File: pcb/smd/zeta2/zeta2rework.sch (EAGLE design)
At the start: 37 parts, among them IC1 MAX6520, IC2 L293DD, U2 INA219, U4 INA219

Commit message: added i2c device
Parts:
- added C10: 0.22µF, rcl:C-EUC0603
- added C12, C43: 47µF, rcl:CPOL-EUSMCC
- added C13, C22: 4.7µF, rcl:C-EUC0603
- added C14: 100µF, rcl:CPOL-EUSMCC
- added C15: 100nF, rcl:C-EUC0603
- added C17: 2,2nF, rcl:C-EUC0603
- added C18, C20, C21: 0.1µF, rcl:C-EUC0603
- added C2: 0.1nF, rcl:C-EUC0603
- added C3, C31, C41: 10nF, rcl:C-EUC0603
- added D3: 1N4004 SMD, diode:DIODE-MELF-MLL41
- added FAN: JST-PH_2-PIN_HEADER, srg:JST-PH_2-PIN_HEADER
- added IC3: L293DD, st-microelectronics:L293DD
- added IRLML2502: (no value), zetex:NMOSSOT23
- added LED: JST-PH_3-PIN_HEADER, srg:JST-PH_3-PIN_HEADER
- added MOTOR_LEFT, RGB_LED: JST-PH_4-PIN_HEADER, srg:JST-PH_4-PIN_HEADER
- added Q1, Q10, Q11, Q3, Q6, Q8, Q9: (no value), semicon-smd-ipc:NPN-TRANSISTOR_SOT23
- added Q5: (no value), semicon-smd-ipc:PNP-TRANSISTOR_SOT23
- added R12, R14, R8: 100k, rcl:R-EU_R0603
- added R13, R5, R6: 500R, rcl:R-EU_R0603
- added R15, R19, R20, R21, R3: 500, rcl:R-EU_R0603
- added R16, R26, R27, R28, R4: 220R, rcl:R-EU_R0603
- added R22: 22R, rcl:R-EU_R0603
- added U$1: RPI-ZERO, rpi-zero:RPI-ZERO
- added U$2: HMC5883L, HMC5883L:HMC5883L
- added U$3: BMP085, BMP085:BMP085
- added U1: MPU-6050, MPU-6050:MPU-6050
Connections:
- new net BMP_EOC: U$3.EOC
- new net HMC_RDY: U$2.DRDY
- new net MPU_INT: U1.INT
- new net M_DIR_2: R13.1, R5.1
- new net N$13: Q5.B, R5.2
- new net N$14: Q6.B, R6.2
- new net N$15: Q8.B, R13.2
- new net N$16: R27.2, RGB_LED.3
- new net N$19: R28.2, RGB_LED.2
- new net N$2: C31.2, IC3.OUT4, MOTOR_LEFT.3
- new net N$22: Q1.B, R3.2
- new net N$23: Q3.B, R19.2
- new net N$24: Q1.E, R28.1
- new net N$25: C3.2, IC3.OUT2, MOTOR_LEFT.1
- new net N$26: C3.1, IC3.OUT1, MOTOR_LEFT.2
- new net N$27: Q10.B, R15.2
- new net N$28: Q3.E, R27.1
- new net N$29: Q9.E, R26.1
- new net N$3: C31.1, IC3.OUT3, MOTOR_LEFT.4
- new net N$30: Q10.E, R4.1
- new net N$31: Q11.B, R21.2
- new net N$32: Q9.B, R20.2
- new net N$33: Q11.E, R16.1
- new net N$34: C17.1, U1.CPOUT
- new net N$35: LED.1, R16.2
- new net N$36: C21.1, U1.REGOUT
- new net N$37: IRLML2502.G, R22.2
- new net N$38: C10.2, U$2.SETC
- new net N$39: C10.1, U$2.SETP
- new net N$4: R26.2, RGB_LED.4
- new net N$40: C13.1, U$2.C1
- new net N$48: LED.2, R4.2
- new net N$55: C41.2, D3.A, FAN.2, IRLML2502.D
- new net N$6: IC3.IN2, IC3.IN3, Q8.C, R8.1
- new net N$7: IC3.IN1, IC3.IN4, Q5.C, R14.2
- new net N$9: IC3.EN1, IC3.EN2, Q6.C, R12.1
- new net PWM_FAN: R22.1
- new net PWM_M_EN_2: R6.1
- new net SCL1: U$2.SCL
- new net SDA1: U$2.SDA
- net +3V3: now also C15.1, C18.1, C20.1, C22.1, U$2.S1, U$2.VDD, U$2.VDDIO, U$3.VDDA, U$3.VDDD, U1.VDD, U1.VLOGIC
- net +5V: now also C14.+, C2.1, IC3.VSS, Q1.C, Q10.C, Q11.C, Q3.C, Q5.E, Q9.C, R12.2, R8.2
- net +8V: now also C12.+, C41.1, C43.+, D3.C, FAN.1, IC3.VS
- net GND: now also C12.-, C13.2, C14.-, C15.2, C17.2, C18.2, C2.2, C20.2, C21.2, C22.2, C43.-, IC3.GND@1, IC3.GND@2, IC3.GND@3, IC3.GND@4, IC3.GND@5, IC3.GND@6, IC3.GND@7, IC3.GND@8, IRLML2502.S, LED.3, Q6.E, Q8.E, R14.1, RGB_LED.1, U$2.GND, U$3.GND, U$3.XCLR, U1.AD0, U1.CLKIN, U1.FSYNC, U1.GND
- net N$17: now also MOTOR_RIGHT.4; no longer MOTOR_RIGHT.3
- net N$18: now also MOTOR_RIGHT.3; no longer MOTOR_RIGHT.4
- net N$20: now also MOTOR_RIGHT.1; no longer MOTOR_RIGHT.2
- net N$21: now also MOTOR_RIGHT.2; no longer MOTOR_RIGHT.1
- net SCL: now also U$3.SCL, U1.SCL
- net SDA: now also U$3.SDA, U1.SDA

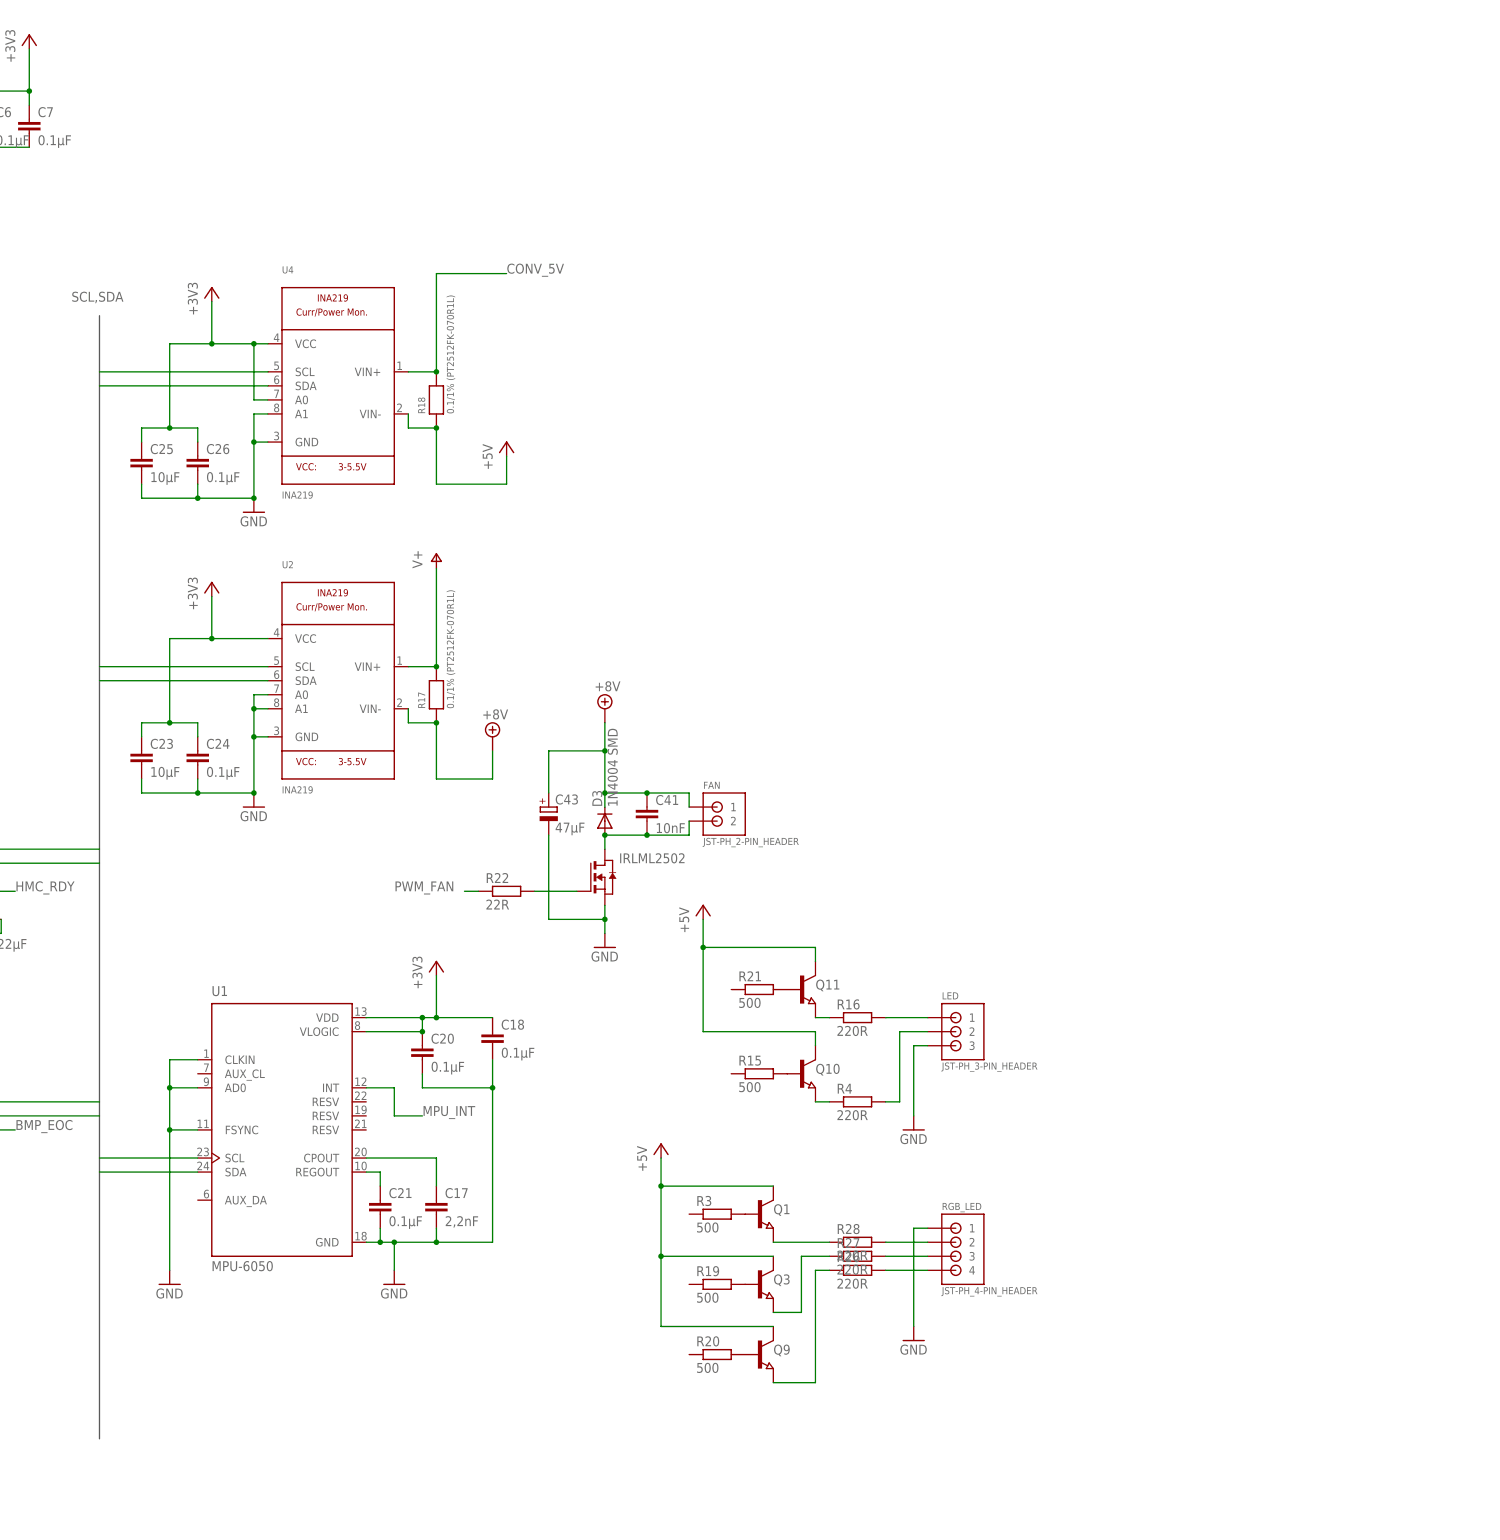
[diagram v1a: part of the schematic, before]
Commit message: worked on pcb, fixed stm32 layout
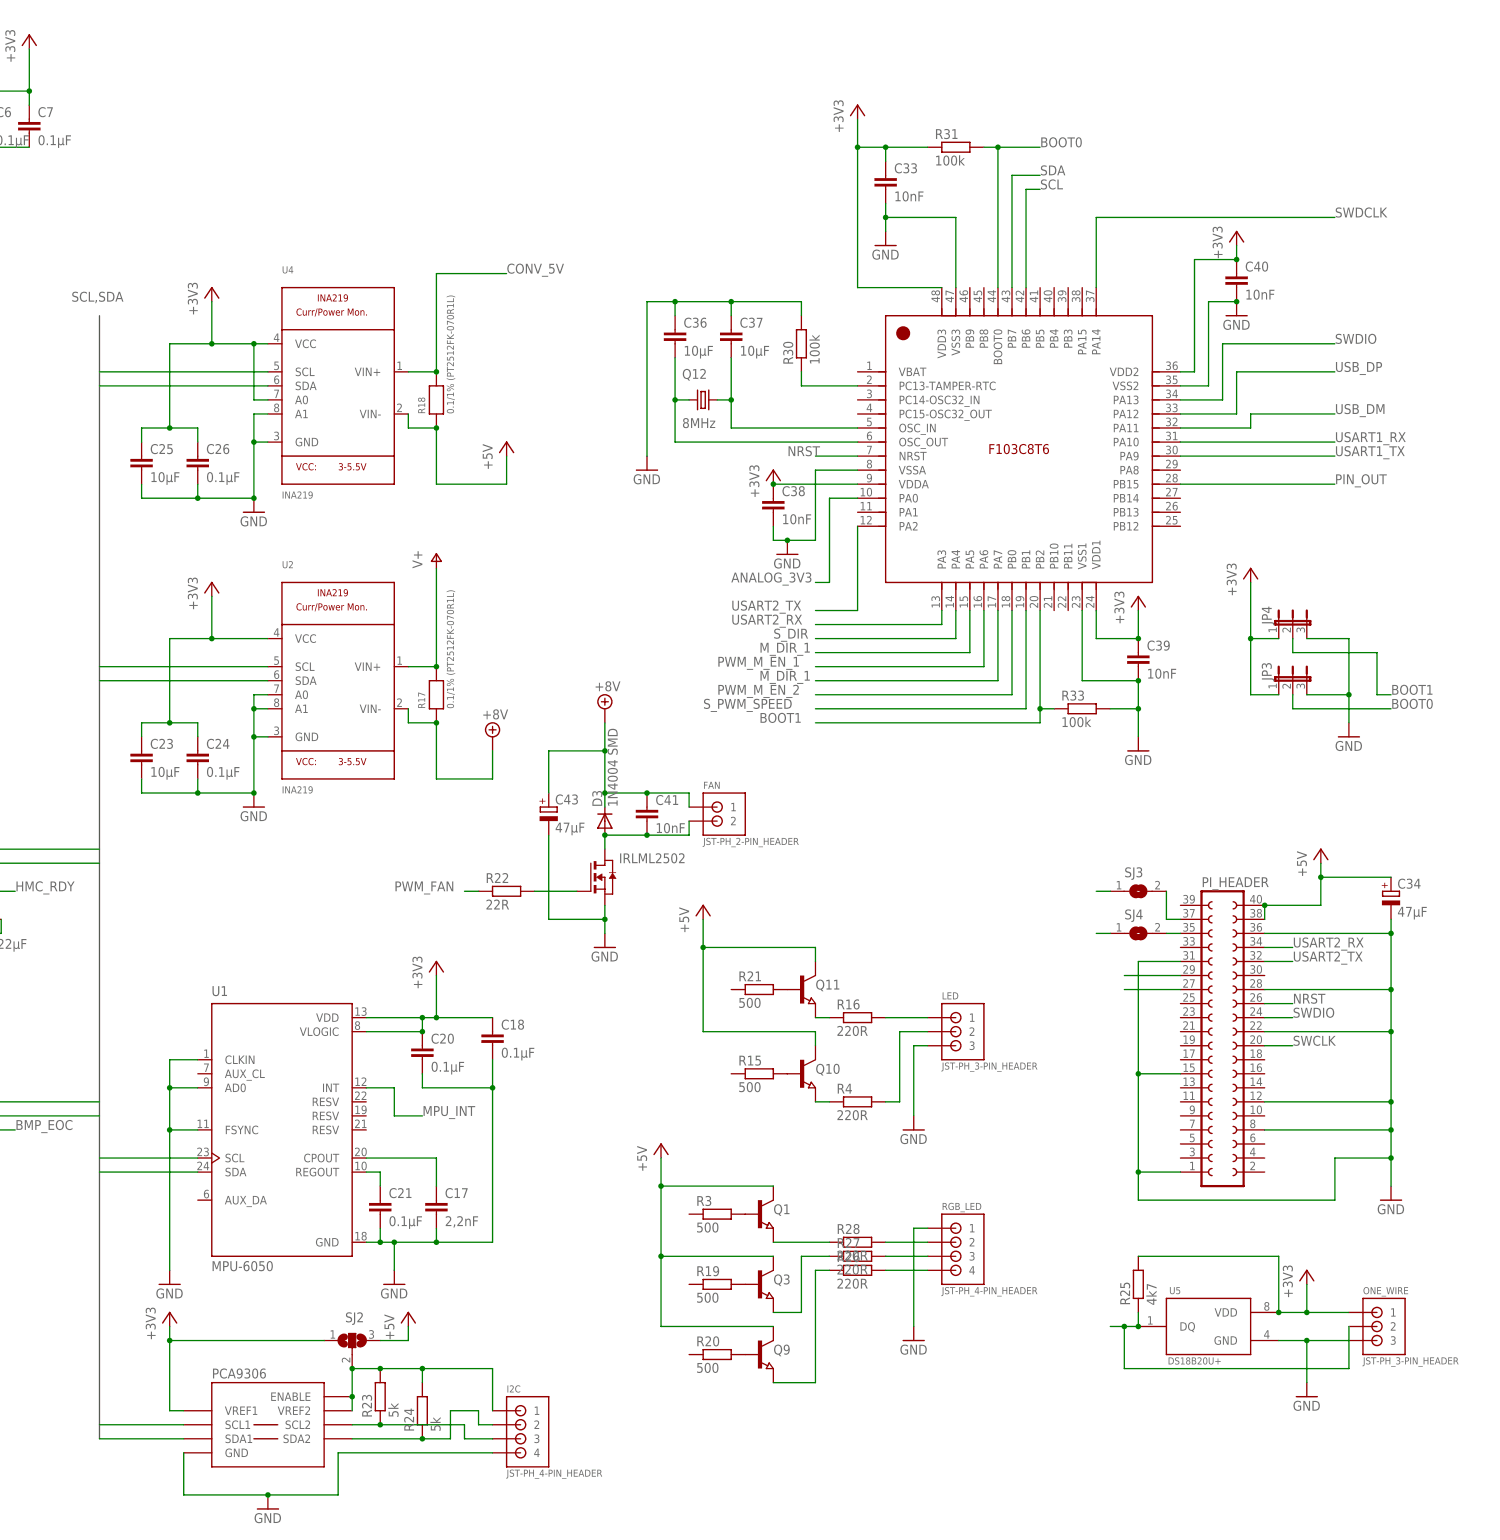
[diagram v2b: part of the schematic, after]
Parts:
- added C33, C38, C39, C40: 10nF, rcl:C-EUC0603
- added C34: 47µF, rcl:CPOL-EUSMCC
- added C36, C37: 10µF, rcl:C-EUC0603
- added I2C: JST-PH_4-PIN_HEADER, srg:JST-PH_4-PIN_HEADER
- added JP3, JP4: (no value), jumper:JP2E
- added ONE_WIRE: JST-PH_3-PIN_HEADER, srg:JST-PH_3-PIN_HEADER
- added PCA9306: (no value), srg:IC2_LEVEL_TRANSLATER
- added PI_HEADER: (no value), con-lsta:FE20-2
- added Q12: 8MHz, crystal-geyer_V1_0:KX-13
- added R23, R24: 5k, rcl:R-EU_R0603
- added R25: 4k7, rcl:R-EU_R0603
- added R30, R31, R33: 100k, rcl:R-EU_R0603
- added SJ2: (no value), jumper:SJ2W
- added SJ3, SJ4: (no value), microbuilder:SOLDERJUMPERREFLOW_NOPASTE
- added U$4: STM32F103C8T6, STM32F103C8T6:STM32F103C8T6
- added U5: DS18B20U+, DS18B20U_:DS18B20U+
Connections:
- new net ANALOG_3V3: U$4.PA0
- new net BOOT0: JP3.2, R31.2, U$4.BOOT0
- new net BOOT1: JP4.2, R33.1, U$4.PB2
- new net BOOT2: PI_HEADER.29
- new net BOOT3: PI_HEADER.27
- new net N$41: I2C.1, PCA9306.ENABLE, PCA9306.VREF2, R23.2, R24.2, SJ2.2
- new net N$42: I2C.3, PCA9306.SCL2, R23.1
- new net N$43: I2C.2, PCA9306.SDA2, R24.1
- new net N$44: PI_HEADER.37, SJ3.2
- new net N$45: PI_HEADER.35, SJ4.2
- new net N$46: C36.2, Q12.1, U$4.OSC_OUT
- new net N$47: C37.2, Q12.2, U$4.OSC_IN
- new net N$49: R30.1, U$4.PC13-TAMPER-RTC
- new net NRST: PI_HEADER.26, U$4.NRST
- new net PIN_OUT: U$4.PB15
- new net SCL2: PCA9306.SCL1
- new net SCL3: SJ4.1
- new net SDA2: PCA9306.SDA1
- new net SDA3: SJ3.1
- new net SWCLK: PI_HEADER.20
- new net SWDCLK: U$4.PA14
- new net SWDIO: PI_HEADER.24, U$4.PA13
- new net S_DIR: U$4.PA4
- new net S_PWM_SPEED: U$4.PB1
- new net TEMPERATURE: ONE_WIRE.2, R25.1, U5.DQ
- new net USART1_RX: U$4.PA10
- new net USART1_TX: U$4.PA9
- new net USART2_RX: PI_HEADER.34, U$4.PA3
- new net USART2_TX: PI_HEADER.32, U$4.PA2
- new net USB_DM: U$4.PA11
- new net USB_DP: U$4.PA12
- net +3V3: now also C33.1, C38.1, C39.1, C40.1, JP3.1, JP4.1, ONE_WIRE.1, PCA9306.VREF1, R25.2, R31.1, SJ2.1, U$4.VDD1, U$4.VDD2, U$4.VDD3, U$4.VDDA, U5.VDD
- net +5V: now also C34.+, PI_HEADER.38, PI_HEADER.40, SJ2.3
- net GND: now also C33.2, C34.-, C36.1, C37.1, C38.2, C39.2, C40.2, I2C.4, JP3.3, JP4.3, ONE_WIRE.3, PCA9306.GND, PI_HEADER.1, PI_HEADER.12, PI_HEADER.15, PI_HEADER.22, PI_HEADER.28, PI_HEADER.31, PI_HEADER.36, PI_HEADER.8, R30.2, R33.2, U$4.VSS1, U$4.VSS2, U$4.VSS3, U$4.VSSA, U5.GND
- net M_DIR_1: now also U$4.PA5, U$4.PA7
- net PWM_M_EN_1: now also U$4.PA6
- net PWM_M_EN_2: now also U$4.PB0
- net SCL: now also U$4.PB6
- net SDA: now also U$4.PB7

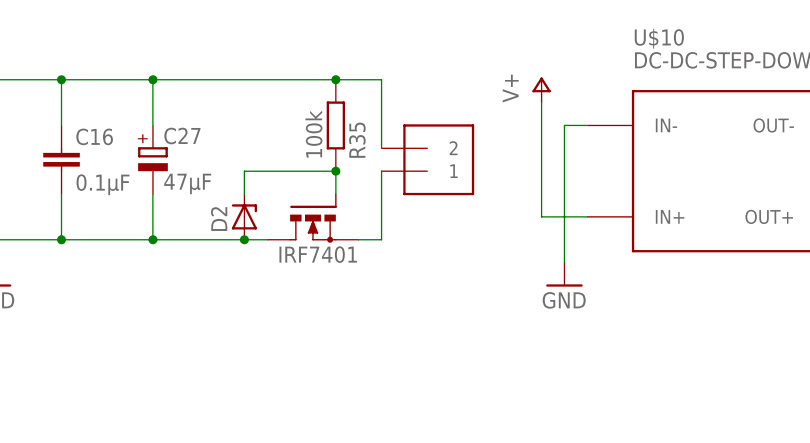
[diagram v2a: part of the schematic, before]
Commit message: worked on pcb layout -piheader wrong
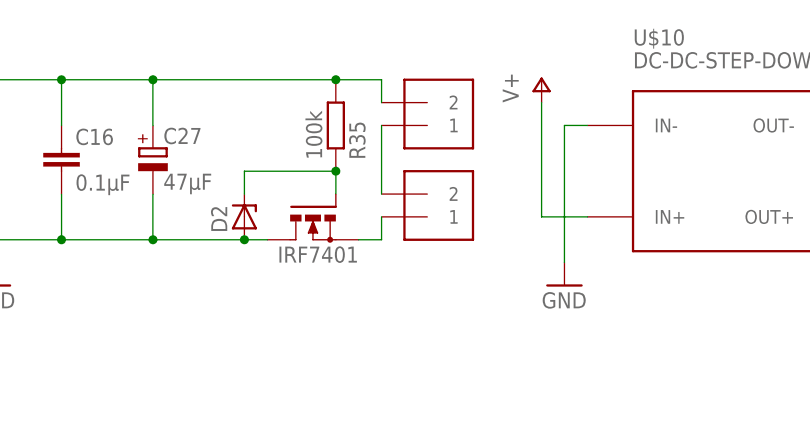
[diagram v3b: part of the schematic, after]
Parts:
- added SUPPLY_IN1: TERMBLOCK_1X2-3.5MM, microbuilder:TERMBLOCK_1X2-3.5MM
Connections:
- new net N$50: SUPPLY_IN.1, SUPPLY_IN1.2
- net N$60: now also SUPPLY_IN1.1; no longer SUPPLY_IN.1
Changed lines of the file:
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@@
 <part name="R25" library="rcl" library_urn="urn:adsk.eagle:library:334" deviceset="R-EU_" device="R0603" package3d_urn="urn:adsk.eagle:package:23555/2" value="4k7"/>
 <part name="ONE_WIRE" library="srg" deviceset="JST-PH_3-PIN_HEADER" device=""/>
+<part name="SUPPLY_IN1" library="microbuilder" deviceset="TERMBLOCK_1X2" device="-3.5MM"/>
 </parts>
 <sheets>
@@
 </instance>
 <instance part="D2" gate="G$1" x="-109.22" y="38.1" rot="R90"/>
-<instance part="SUPPLY_IN" gate="G$1" x="-88.9" y="45.72" rot="MR180"/>
+<instance part="SUPPLY_IN" gate="G$1" x="-88.9" y="50.8" rot="MR180"/>
 <instance part="GND1" gate="1" x="-73.66" y="30.48"/>
 <instance part="IC1" gate="-1" x="0" y="45.72"/>
@@
 <instance part="R25" gate="G$1" x="238.76" y="-170.18" rot="R90"/>
 <instance part="ONE_WIRE" gate="G$1" x="281.94" y="-177.8"/>
+<instance part="SUPPLY_IN1" gate="G$1" x="-88.9" y="40.64" rot="MR180"/>
 </instances>
 <busses>
@@
 <pinref part="P+13" gate="1" pin="V+"/>
 <wire x1="-142.24" y1="55.88" x2="-142.24" y2="53.34" width="0.1524" layer="91"/>
-<pinref part="SUPPLY_IN" gate="G$1" pin="2"/>
-<wire x1="-93.98" y1="53.34" x2="-93.98" y2="45.72" width="0.1524" layer="91"/>
 <pinref part="R35" gate="G$1" pin="2"/>
-<wire x1="-93.98" y1="53.34" x2="-99.06" y2="53.34" width="0.1524" layer="91"/>
 <pinref part="C27" gate="G$1" pin="+"/>
 <wire x1="-119.38" y1="48.26" x2="-119.38" y2="53.34" width="0.1524" layer="91"/>
 <wire x1="-119.38" y1="53.34" x2="-99.06" y2="53.34" width="0.1524" layer="91"/>
-<junction x="-99.06" y="53.34"/>
 <pinref part="C16" gate="G$1" pin="1"/>
 <wire x1="-129.54" y1="48.26" x2="-129.54" y2="53.34" width="0.1524" layer="91"/>
@@
 <wire x1="-142.24" y1="53.34" x2="-129.54" y2="53.34" width="0.1524" layer="91"/>
 <junction x="-129.54" y="53.34"/>
+<wire x1="-99.06" y1="53.34" x2="-93.98" y2="53.34" width="0.1524" layer="91"/>
+<junction x="-99.06" y="53.34"/>
+<pinref part="SUPPLY_IN" gate="G$1" pin="2"/>
+<wire x1="-93.98" y1="53.34" x2="-93.98" y2="50.8" width="0.1524" layer="91"/>
 </segment>
 <segment>
@@
 <net name="N$60" class="0">
 <segment>
-<pinref part="SUPPLY_IN" gate="G$1" pin="1"/>
-<wire x1="-93.98" y1="43.18" x2="-93.98" y2="35.56" width="0.1524" layer="91"/>
 <pinref part="IRF7401" gate="G$1" pin="S"/>
 <wire x1="-96.52" y1="35.56" x2="-93.98" y2="35.56" width="0.1524" layer="91"/>
+<pinref part="SUPPLY_IN1" gate="G$1" pin="1"/>
+<wire x1="-93.98" y1="35.56" x2="-93.98" y2="38.1" width="0.1524" layer="91"/>
 </segment>
 </net>
@@
 </segment>
 </net>
+<net name="N$50" class="0">
+<segment>
+<pinref part="SUPPLY_IN1" gate="G$1" pin="2"/>
+<pinref part="SUPPLY_IN" gate="G$1" pin="1"/>
+<wire x1="-93.98" y1="40.64" x2="-93.98" y2="48.26" width="0.1524" layer="91"/>
+</segment>
+</net>
